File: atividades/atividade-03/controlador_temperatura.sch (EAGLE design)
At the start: 32 parts, among them Q1 BC337, Q2 BC337, Q3 BC337

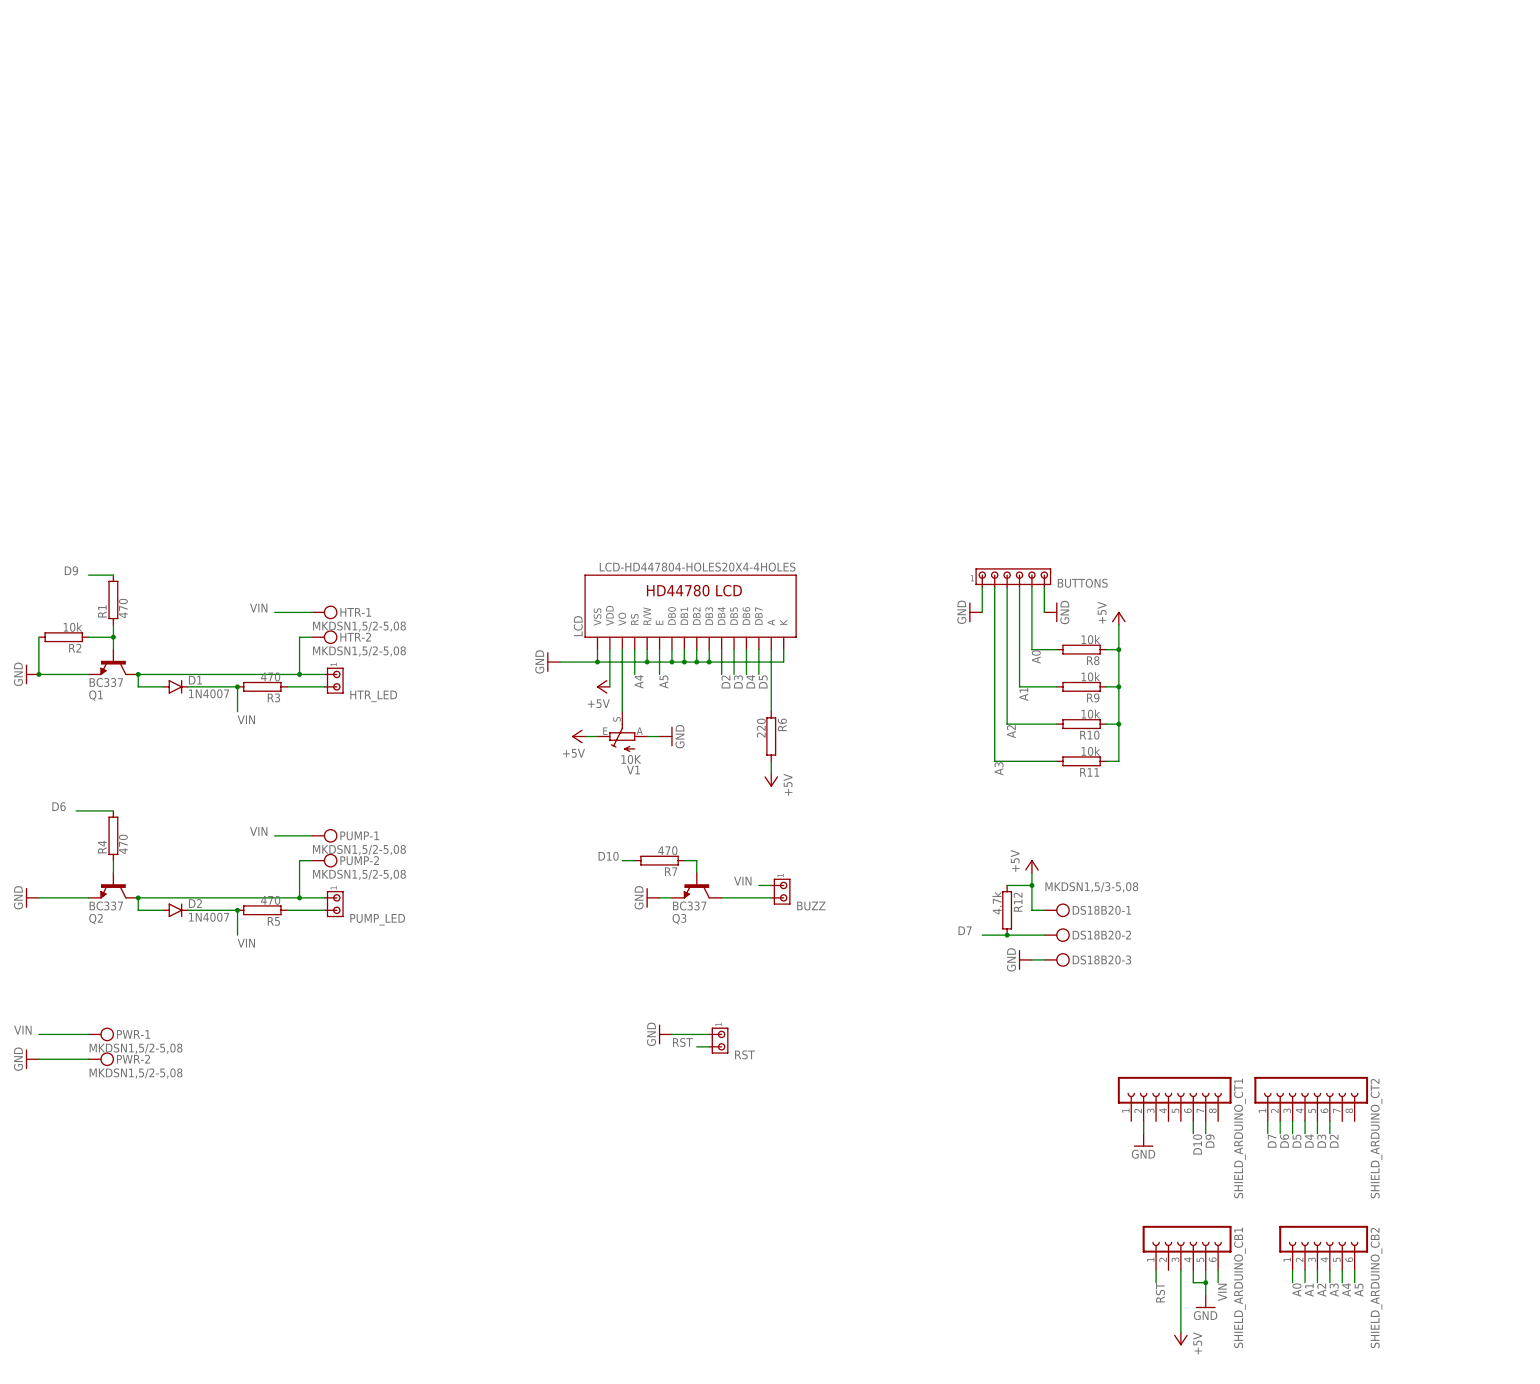
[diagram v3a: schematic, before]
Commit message: display scheme corrigido
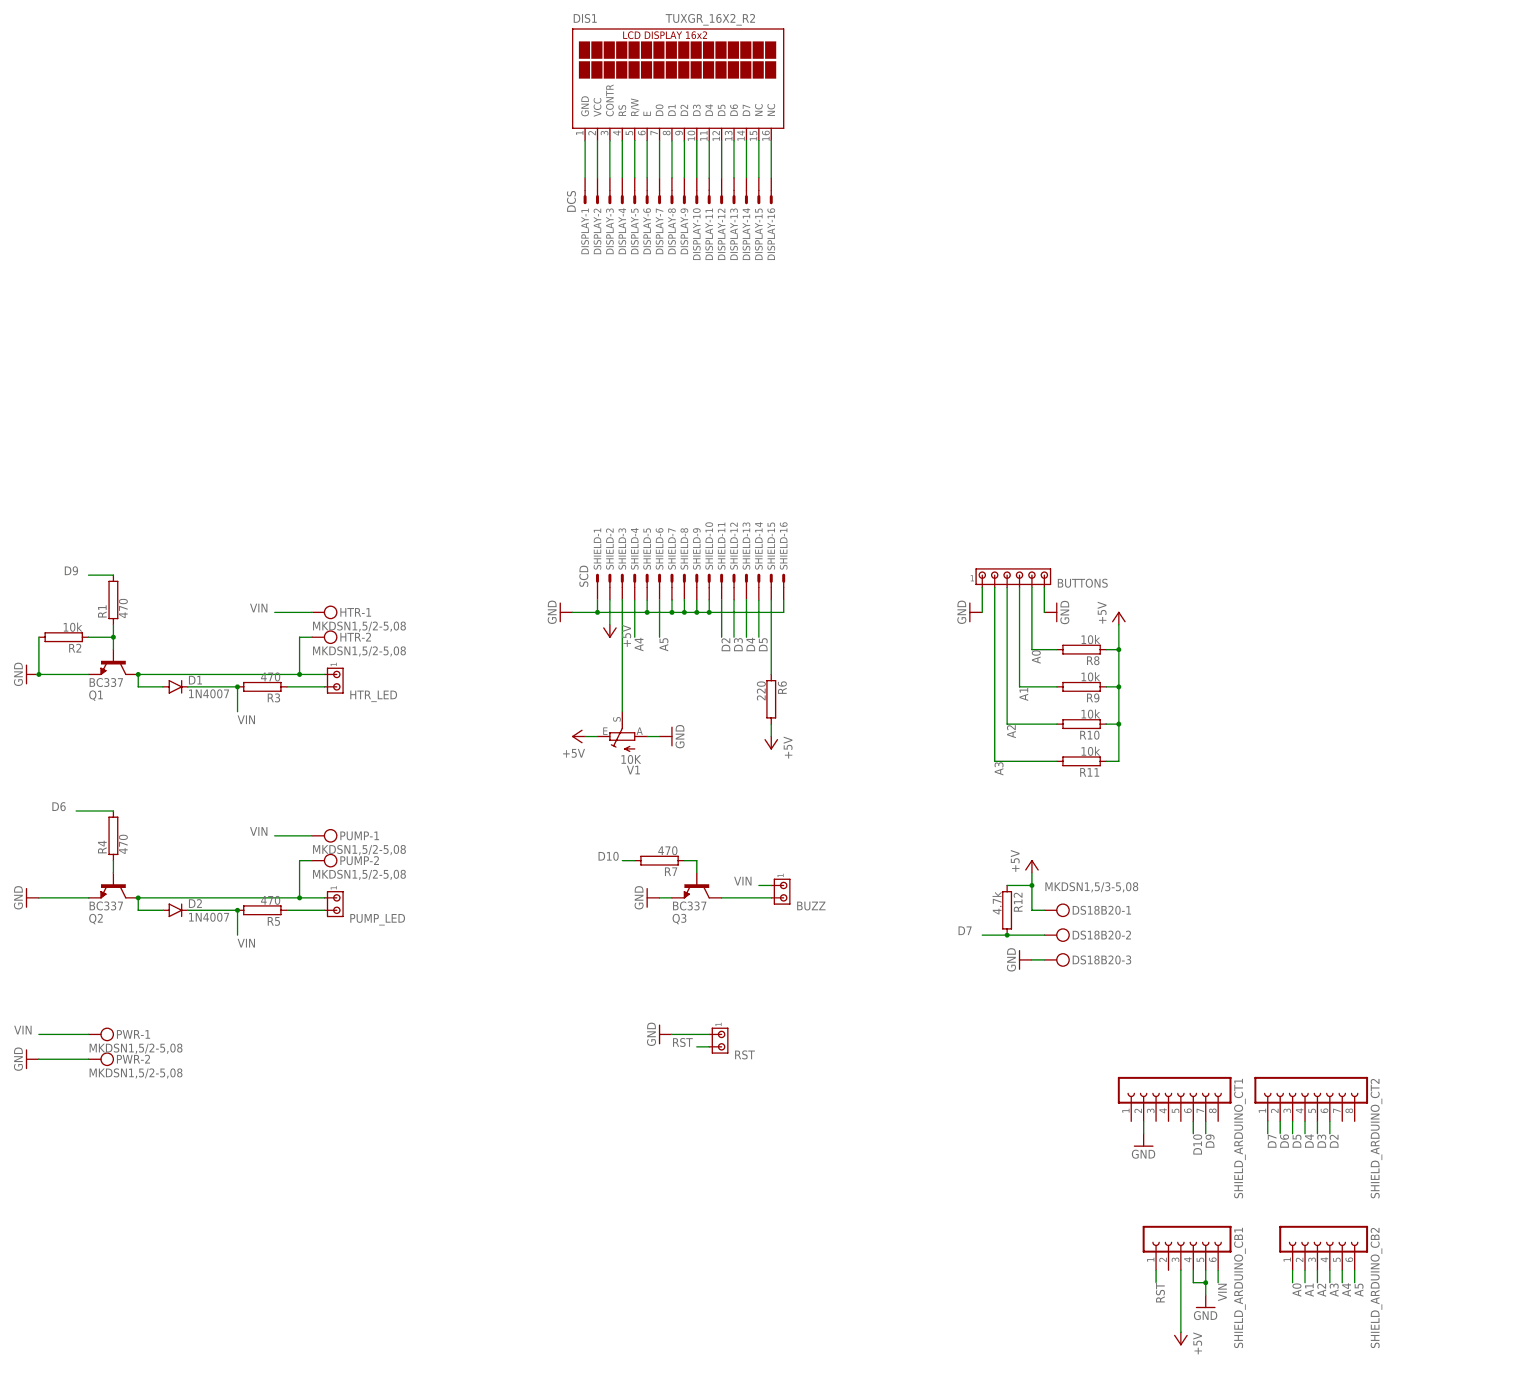
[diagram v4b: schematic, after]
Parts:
- removed LCD: LCD-HD447804-HOLES20X4-4HOLES, HD44780LCD:LCD-HD447804-HOLES20X4-4HOLES
- added DIS1: TUXGR_16X2_R2, display-lcd:TUXGR_16X2_R2
- added DISPLAY: DCS, con-panduit:057-016-1
- added SHIELD: SCD, con-panduit:057-016-1
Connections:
- new net N$10: DIS1.VCC, DISPLAY-2.S
- new net N$11: DIS1.CONTR, DISPLAY-3.S
- new net N$12: DIS1.RS, DISPLAY-4.S
- new net N$13: DIS1.R/W, DISPLAY-5.S
- new net N$15: DIS1.D0, DISPLAY-7.S
- new net N$16: DIS1.D1, DISPLAY-8.S
- new net N$17: DIS1.D2, DISPLAY-9.S
- new net N$18: DIS1.D3, DISPLAY-10.S
- new net N$19: DIS1.D4, DISPLAY-11.S
- new net N$20: DIS1.D5, DISPLAY-12.S
- new net N$21: DIS1.D6, DISPLAY-13.S
- new net N$22: DIS1.D7, DISPLAY-14.S
- new net N$23: DIS1.NC@1, DISPLAY-15.S
- new net N$24: DIS1.NC@2, DISPLAY-16.S
- new net N$25: R6.1, SHIELD-15.S
- new net N$26: SHIELD-3.S, V1.S
- net A4: now also SHIELD-4.S; no longer LCD.RS
- net A5: now also SHIELD-6.S; no longer LCD.E
- net D2: now also SHIELD-11.S; no longer LCD.DB4
- net D3: now also SHIELD-12.S; no longer LCD.DB5
- net D4: now also SHIELD-13.S; no longer LCD.DB6
- net D5: now also SHIELD-14.S; no longer LCD.DB7
- net GND: now also SHIELD-1.S, SHIELD-10.S, SHIELD-16.S, SHIELD-5.S, SHIELD-7.S, SHIELD-8.S, SHIELD-9.S; no longer LCD.DB0, LCD.DB1, LCD.DB2, LCD.DB3, LCD.K, LCD.R/W, LCD.VSS
- net N$14: now also DIS1.E, DISPLAY-6.S; no longer LCD.A, R6.1
- net N$7: now also DIS1.GND, DISPLAY-1.S; no longer LCD.VO, V1.S
- net VCC: now also SHIELD-2.S; no longer LCD.VDD
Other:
- moved on the sheet: R6

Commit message: organizando posições do schema
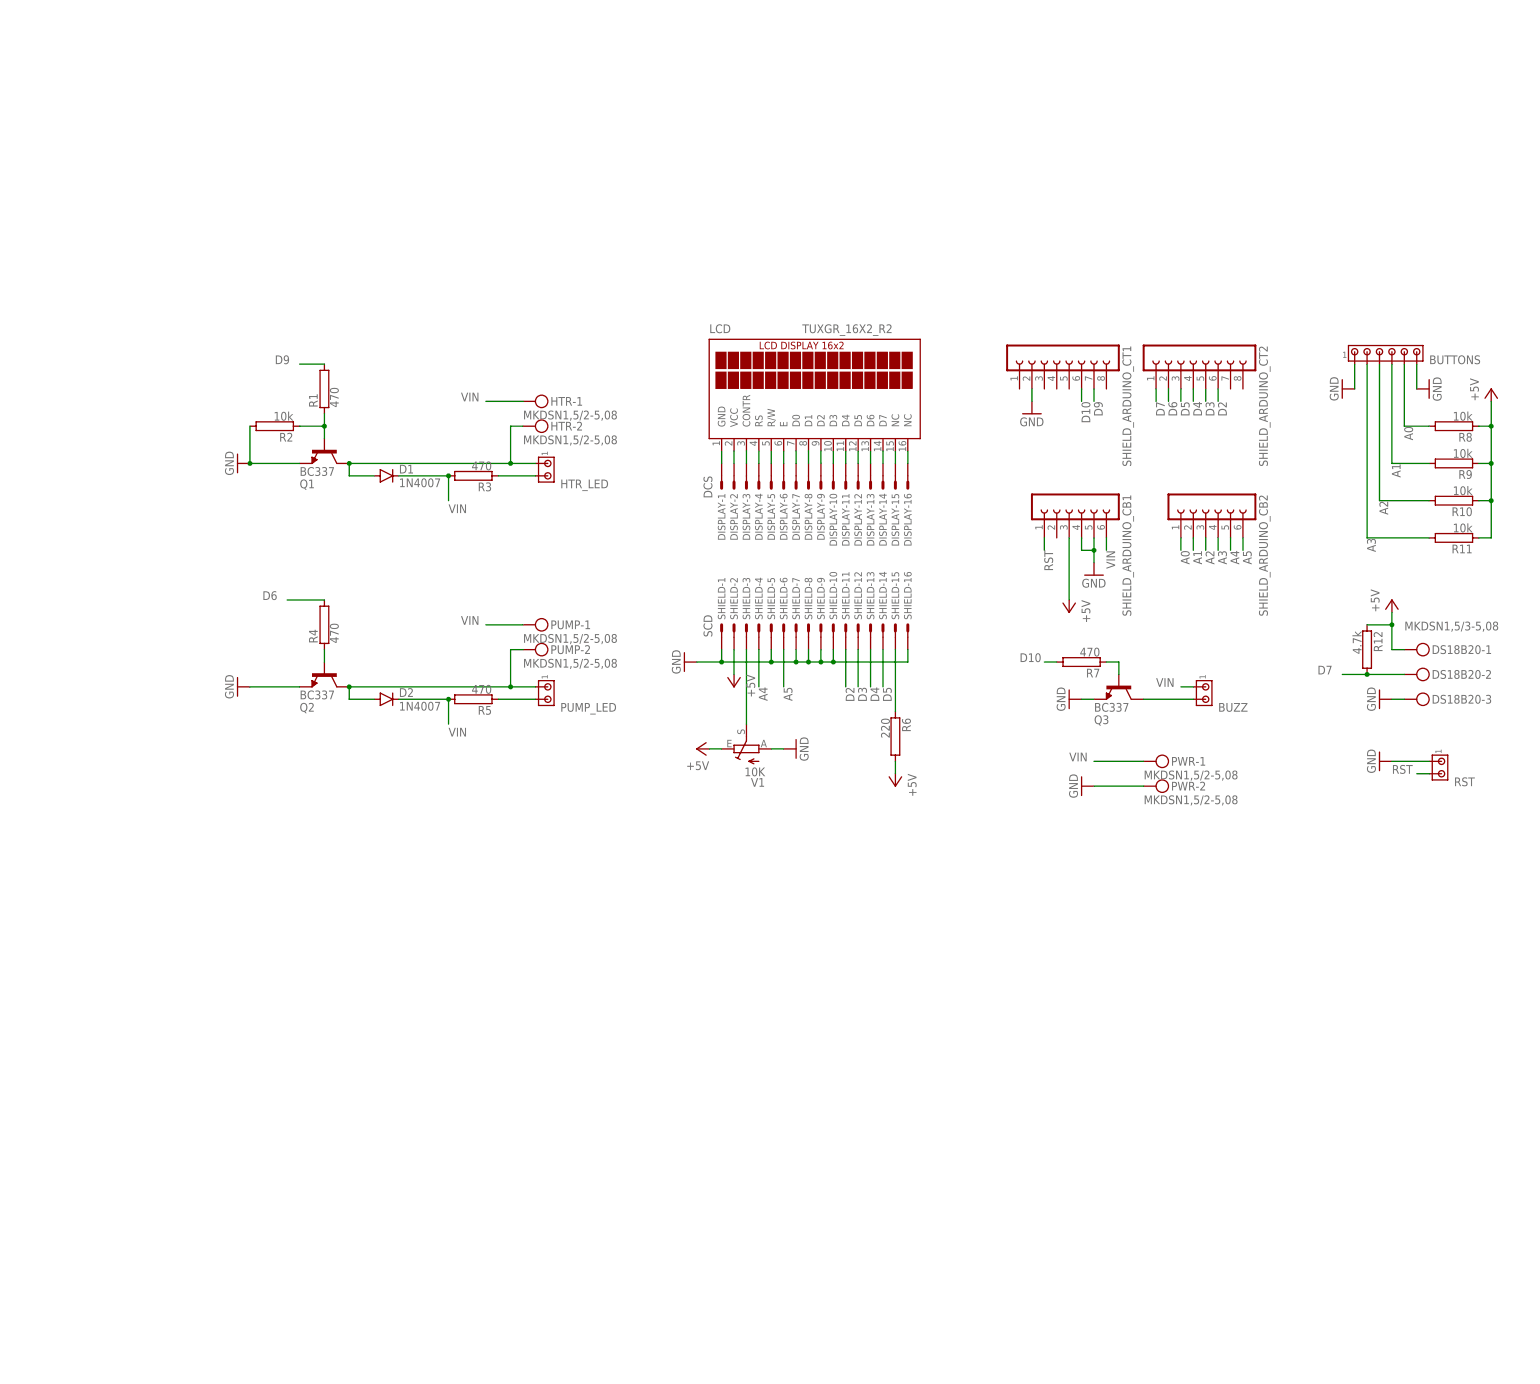
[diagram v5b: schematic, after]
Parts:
- removed DIS1: TUXGR_16X2_R2, display-lcd:TUXGR_16X2_R2
- added LCD: TUXGR_16X2_R2, display-lcd:TUXGR_16X2_R2
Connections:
- net N$10: now also LCD.VCC; no longer DIS1.VCC
- net N$11: now also LCD.CONTR; no longer DIS1.CONTR
- net N$12: now also LCD.RS; no longer DIS1.RS
- net N$13: now also LCD.R/W; no longer DIS1.R/W
- net N$14: now also LCD.E; no longer DIS1.E
- net N$15: now also LCD.D0; no longer DIS1.D0
- net N$16: now also LCD.D1; no longer DIS1.D1
- net N$17: now also LCD.D2; no longer DIS1.D2
- net N$18: now also LCD.D3; no longer DIS1.D3
- net N$19: now also LCD.D4; no longer DIS1.D4
- net N$20: now also LCD.D5; no longer DIS1.D5
- net N$21: now also LCD.D6; no longer DIS1.D6
- net N$22: now also LCD.D7; no longer DIS1.D7
- net N$23: now also LCD.NC@1; no longer DIS1.NC@1
- net N$24: now also LCD.NC@2; no longer DIS1.NC@2
- net N$7: now also LCD.GND; no longer DIS1.GND
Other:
- moved on the sheet: BUTTONS, BUZZ, D1, D2, DISPLAY-1, DISPLAY-10, DISPLAY-11, DISPLAY-12, DISPLAY-13, DISPLAY-14, DISPLAY-15, DISPLAY-16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
